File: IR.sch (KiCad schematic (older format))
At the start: 6 parts, among them U47 74LS245, U48 74LS173, U49 74LS173, U50 74LS245, U51 74LS173, U52 74LS173

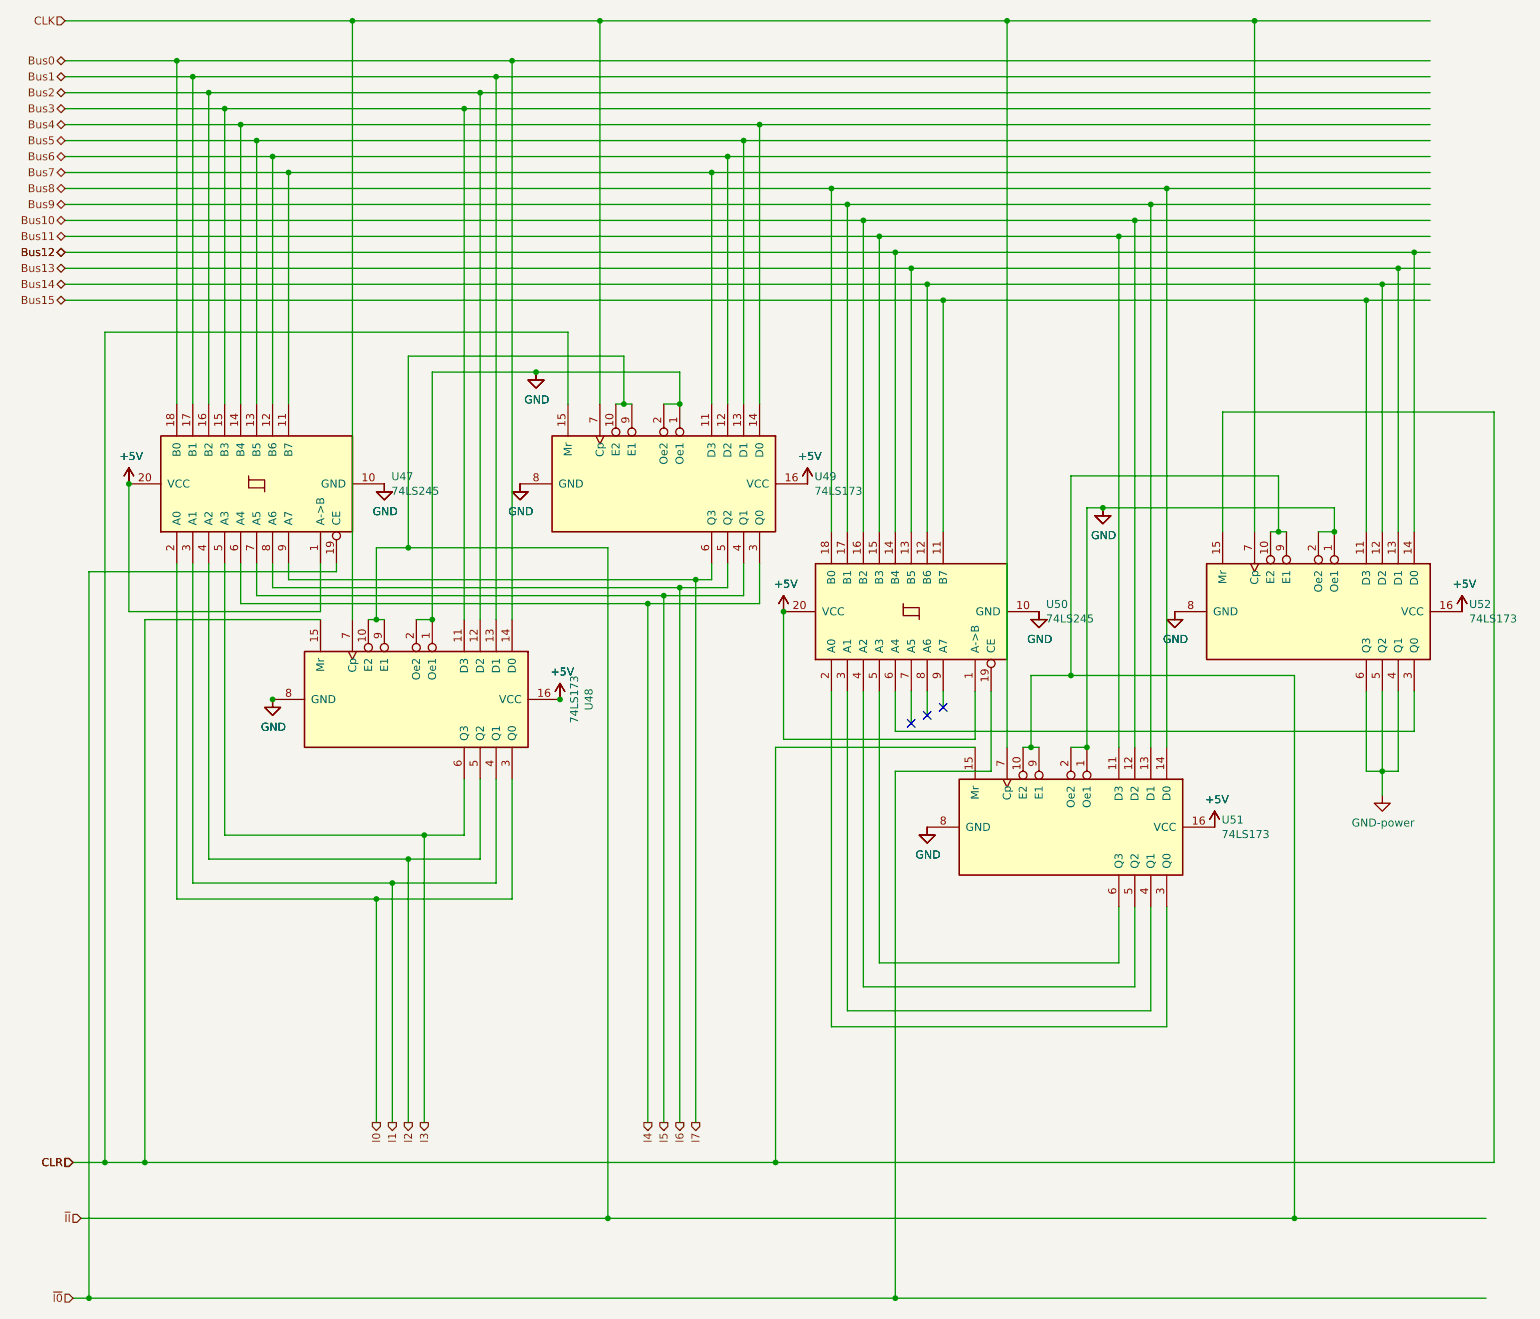
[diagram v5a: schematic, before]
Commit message: Made IR & Stack 12 bits
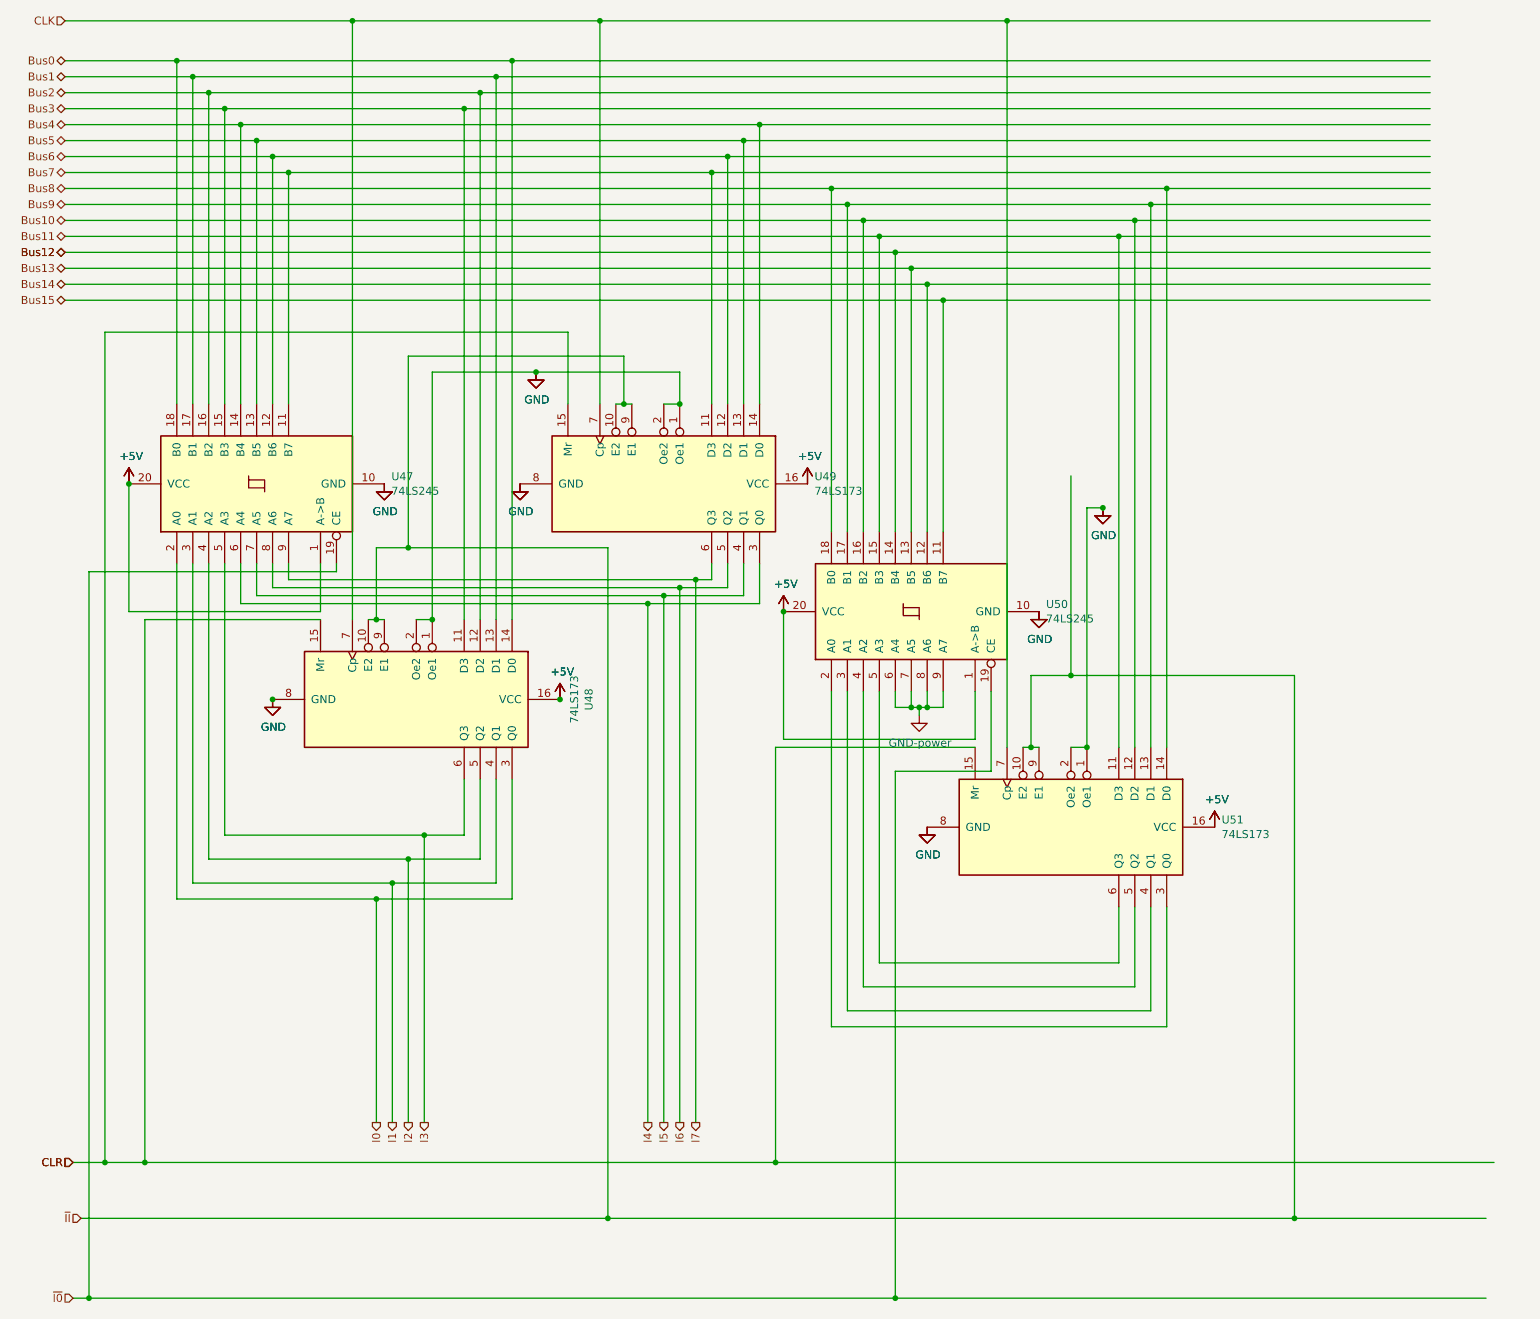
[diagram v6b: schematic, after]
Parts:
- removed U52: 74LS173, Package_DIP:DIP-16_W7.62mm, symbol 16bitCpu-rescue:74LS173-74xx
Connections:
- wire segments 219 -> 196
- no-connect marks 3 -> 0
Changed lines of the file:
@@
 	7050 6900 7050 5200
-Wire Wire Line
-	7150 5200 7150 5450
-Wire Wire Line
-	10400 5450 10400 5200
-Wire Wire Line
-	7250 5200 7250 5400
-Wire Wire Line
-	7350 5350 7350 5200
-Wire Wire Line
-	7450 5200 7450 5300
 Wire Wire Line
 	8550 5550 8550 2350
@@
 F 3 "" H 8050 4700 50  0001 C CNN
 	1    8050 4700
-	1    0    0    -1
-$EndComp
-$Comp
-L 16bitCpu-rescue:GND-power #PWR?
-U 1 1 5F7C1DCB
-P 8900 4700
-AR Path="/5F7C1DCB" Ref="#PWR?"  Part="1"
-AR Path="/5F67C726/5F7C1DCB" Ref="#PWR?"  Part="1"
-AR Path="/5F70885A/5F7C1DCB" Ref="#PWR?"  Part="1"
-AR Path="/5F733C5E/5F7C1DCB" Ref="#PWR?"  Part="1"
-AR Path="/602D4838/5F7C1DCB" Ref="#PWR?"  Part="1"
-AR Path="/603B00C8/5F7C1DCB" Ref="#PWR?"  Part="1"
-AR Path="/603B766D/5F7C1DCB" Ref="#PWR?"  Part="1"
-AR Path="/5F74778C/5F7C1DCB" Ref="#PWR?"  Part="1"
-AR Path="/5F79B702/5F7C1DCB" Ref="#PWR0164"  Part="1"
-F 0 "#PWR0164" H 8900 4450 50  0001 C CNN
-F 1 "GND" H 8905 4527 50  0000 C CNN
-F 2 "" H 8900 4700 50  0001 C CNN
-F 3 "" H 8900 4700 50  0001 C CNN
-	1    8900 4700
 	1    0    0    -1
 $EndComp
@@
 $Comp
 L 16bitCpu-rescue:+5V-power #PWR?
-U 1 1 5F7C1DFB
-P 10700 4700
-AR Path="/5F7C1DFB" Ref="#PWR?"  Part="1"
-AR Path="/5F67C726/5F7C1DFB" Ref="#PWR?"  Part="1"
-AR Path="/5F70885A/5F7C1DFB" Ref="#PWR?"  Part="1"
-AR Path="/5F733C5E/5F7C1DFB" Ref="#PWR?"  Part="1"
-AR Path="/602D4838/5F7C1DFB" Ref="#PWR?"  Part="1"
-AR Path="/603B00C8/5F7C1DFB" Ref="#PWR?"  Part="1"
-AR Path="/603B766D/5F7C1DFB" Ref="#PWR?"  Part="1"
-AR Path="/5F74778C/5F7C1DFB" Ref="#PWR?"  Part="1"
-AR Path="/5F79B702/5F7C1DFB" Ref="#PWR0168"  Part="1"
-F 0 "#PWR0168" H 10700 4550 50  0001 C CNN
-F 1 "+5V" H 10715 4873 50  0000 C CNN
-F 2 "" H 10700 4700 50  0001 C CNN
-F 3 "" H 10700 4700 50  0001 C CNN
-	1    10700 4700
-	1    0    0    -1
-$EndComp
-$Comp
-L 16bitCpu-rescue:+5V-power #PWR?
 U 1 1 5F7C1E01
 P 6600 3900
@@
 Wire Wire Line
 	8350 4050 8450 4050
-Wire Wire Line
-	9900 4050 9900 4200
 Connection ~ 8350 5550
-Wire Wire Line
-	9800 4200 9900 4200
-Connection ~ 9900 4200
 $Comp
 L 16bitCpu-rescue:GND-power #PWR?
@@
 Connection ~ 8450 4050
 Wire Wire Line
-	8450 4050 9900 4050
-Wire Wire Line
 	7850 5550 7850 1000
-Wire Wire Line
-	7850 1000 9400 1000
 Connection ~ 7850 1000
-Wire Wire Line
-	9400 4200 9400 1000
-Connection ~ 9400 1000
-Wire Wire Line
-	9400 1000 10500 1000
 Wire Wire Line
 	5300 3400 5300 1000
@@
 Connection ~ 6400 8150
 Wire Wire Line
-	9200 4200 9200 3450
-Wire Wire Line
-	9200 3450 10900 3450
-Wire Wire Line
 	6400 8150 10900 8150
 Wire Wire Line
@@
 Wire Wire Line
 	8250 5100 8250 3850
-Wire Wire Line
-	8250 3850 9550 3850
-Wire Wire Line
-	9550 3850 9550 4200
-Wire Wire Line
-	9550 4200 9600 4200
 Connection ~ 8000 5550
 Wire Wire Line
 	8000 5550 8050 5550
-Wire Wire Line
-	9550 4200 9500 4200
-Connection ~ 9550 4200
 Wire Wire Line
 	3850 4750 3900 4750
@@
 $EndComp
 $Comp
-L 16bitCpu-rescue:74LS173-74xx U?
-U 1 1 5F7C1E93
-P 9800 4700
-AR Path="/5F7C1E93" Ref="U?"  Part="1"
-AR Path="/5F67C726/5F7C1E93" Ref="U?"  Part="1"
-AR Path="/5F70885A/5F7C1E93" Ref="U?"  Part="1"
-AR Path="/5F733C5E/5F7C1E93" Ref="U?"  Part="1"
-AR Path="/602D4838/5F7C1E93" Ref="U?"  Part="1"
-AR Path="/603B00C8/5F7C1E93" Ref="U?"  Part="1"
-AR Path="/603B766D/5F7C1E93" Ref="U?"  Part="1"
-AR Path="/5F74778C/5F7C1E93" Ref="U?"  Part="1"
-AR Path="/5F79B702/5F7C1E93" Ref="U52"  Part="1"
-F 0 "U52" V 9754 5644 50  0000 L CNN
-F 1 "74LS173" V 9845 5644 50  0000 L CNN
-F 2 "Package_DIP:DIP-16_W7.62mm" H 9800 4700 50  0001 C CNN
-F 3 "http://www.ti.com/lit/gpn/sn74LS173" H 9800 4700 50  0001 C CNN
-	1    9800 4700
-	0    1    1    0
-$EndComp
-$Comp
 L 16bitCpu-rescue:GND-power #PWR?
 U 1 1 5F7C1E99
@@
 F 3 "" H 8050 4700 50  0001 C CNN
 	1    8050 4700
-	1    0    0    -1
-$EndComp
-$Comp
-L 16bitCpu-rescue:GND-power #PWR?
-U 1 1 5F7C1E9F
-P 8900 4700
-AR Path="/5F7C1E9F" Ref="#PWR?"  Part="1"
-AR Path="/5F67C726/5F7C1E9F" Ref="#PWR?"  Part="1"
-AR Path="/5F70885A/5F7C1E9F" Ref="#PWR?"  Part="1"
-AR Path="/5F733C5E/5F7C1E9F" Ref="#PWR?"  Part="1"
-AR Path="/602D4838/5F7C1E9F" Ref="#PWR?"  Part="1"
-AR Path="/603B00C8/5F7C1E9F" Ref="#PWR?"  Part="1"
-AR Path="/603B766D/5F7C1E9F" Ref="#PWR?"  Part="1"
-AR Path="/5F74778C/5F7C1E9F" Ref="#PWR?"  Part="1"
-AR Path="/5F79B702/5F7C1E9F" Ref="#PWR0165"  Part="1"
-F 0 "#PWR0165" H 8900 4450 50  0001 C CNN
-F 1 "GND" H 8905 4527 50  0000 C CNN
-F 2 "" H 8900 4700 50  0001 C CNN
-F 3 "" H 8900 4700 50  0001 C CNN
-	1    8900 4700
 	1    0    0    -1
 $EndComp
@@
 F 3 "" H 9150 6050 50  0001 C CNN
 	1    9150 6050
-	1    0    0    -1
-$EndComp
-$Comp
-L 16bitCpu-rescue:+5V-power #PWR?
-U 1 1 5F7C1ED5
-P 10700 4700
-AR Path="/5F7C1ED5" Ref="#PWR?"  Part="1"
-AR Path="/5F67C726/5F7C1ED5" Ref="#PWR?"  Part="1"
-AR Path="/5F70885A/5F7C1ED5" Ref="#PWR?"  Part="1"
-AR Path="/5F733C5E/5F7C1ED5" Ref="#PWR?"  Part="1"
-AR Path="/602D4838/5F7C1ED5" Ref="#PWR?"  Part="1"
-AR Path="/603B00C8/5F7C1ED5" Ref="#PWR?"  Part="1"
-AR Path="/603B766D/5F7C1ED5" Ref="#PWR?"  Part="1"
-AR Path="/5F74778C/5F7C1ED5" Ref="#PWR?"  Part="1"
-AR Path="/5F79B702/5F7C1ED5" Ref="#PWR0169"  Part="1"
-F 0 "#PWR0169" H 10700 4550 50  0001 C CNN
-F 1 "+5V" H 10715 4873 50  0000 C CNN
-F 2 "" H 10700 4700 50  0001 C CNN
-F 3 "" H 10700 4700 50  0001 C CNN
-	1    10700 4700
 	1    0    0    -1
 $EndComp
@@
 Connection ~ 5050 5250
 Connection ~ 3250 5250
-Wire Wire Line
-	10900 3450 10900 8150
 $Comp
 L 16bitCpu-rescue:74LS173-74xx U?
@@
 	7050 6900 8550 6900
 Wire Wire Line
-	7150 5450 10400 5450
-Wire Wire Line
-	7150 2450 10400 2450
-Wire Wire Line
-	7250 2550 10300 2550
-Wire Wire Line
 	1950 1550 2950 1550
-Wire Wire Line
-	7450 2750 10100 2750
-Wire Wire Line
-	7350 2650 10200 2650
-Wire Wire Line
-	10400 4200 10400 2450
-Connection ~ 10400 2450
-Wire Wire Line
-	10400 2450 10500 2450
-Wire Wire Line
-	10100 5700 10200 5700
-Wire Wire Line
-	10200 5200 10200 5700
-Wire Wire Line
-	10100 5200 10100 5700
-Wire Wire Line
-	10300 5700 10200 5700
-Wire Wire Line
-	10300 5200 10300 5700
-Connection ~ 10200 5700
-Wire Wire Line
-	10200 5700 10200 5850
 $Comp
 L 16bitCpu-rescue:GND-power #PWR0182
 U 1 1 60F44F5B
-P 10200 5850
-F 0 "#PWR0182" H 10200 5600 50  0001 C CNN
-F 1 "GND-power" H 10205 5677 50  0000 C CNN
-F 2 "" H 10200 5850 50  0001 C CNN
-F 3 "" H 10200 5850 50  0001 C CNN
-	1    10200 5850
-	1    0    0    -1
-$EndComp
-Wire Wire Line
-	10300 2550 10300 4200
-Connection ~ 10300 2550
-Wire Wire Line
-	10300 2550 10500 2550
-Wire Wire Line
-	10200 4200 10200 2650
-Connection ~ 10200 2650
-Wire Wire Line
-	10200 2650 10500 2650
-Wire Wire Line
-	10100 4200 10100 2750
-Connection ~ 10100 2750
-Wire Wire Line
-	10100 2750 10500 2750
-NoConn ~ 7250 5400
-NoConn ~ 7350 5350
-NoConn ~ 7450 5300
+P 7300 5350
+F 0 "#PWR0182" H 7300 5100 50  0001 C CNN
+F 1 "GND-power" H 7305 5177 50  0000 C CNN
+F 2 "" H 7300 5350 50  0001 C CNN
+F 3 "" H 7300 5350 50  0001 C CNN
+	1    7300 5350
+	1    0    0    -1
+$EndComp
+Wire Wire Line
+	7150 2450 10500 2450
+Wire Wire Line
+	7250 2550 10500 2550
+Wire Wire Line
+	7350 2650 10500 2650
+Wire Wire Line
+	7450 2750 10500 2750
+Wire Wire Line
+	7850 1000 10500 1000
+Wire Wire Line
+	7150 5200 7150 5300
+Wire Wire Line
+	7150 5300 7250 5300
+Wire Wire Line
+	7250 5300 7250 5200
+Wire Wire Line
+	7250 5300 7300 5300
+Wire Wire Line
+	7350 5300 7350 5200
+Connection ~ 7250 5300
+Wire Wire Line
+	7350 5300 7450 5300
+Wire Wire Line
+	7450 5300 7450 5200
+Connection ~ 7350 5300
+Wire Wire Line
+	7300 5350 7300 5300
+Connection ~ 7300 5300
+Wire Wire Line
+	7300 5300 7350 5300
 $EndSCHEMATC
